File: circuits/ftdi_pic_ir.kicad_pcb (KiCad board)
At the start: 2 copper layers, 33 x 45.7 mm, 20 parts, among them P1 CONN_6, P2 CONN_2, P3 CONN_2, P4 CONN_2, P5 CONN_2, Q1 MOSFET_N, Q2 MOSFET_N, U1 PIC12F683

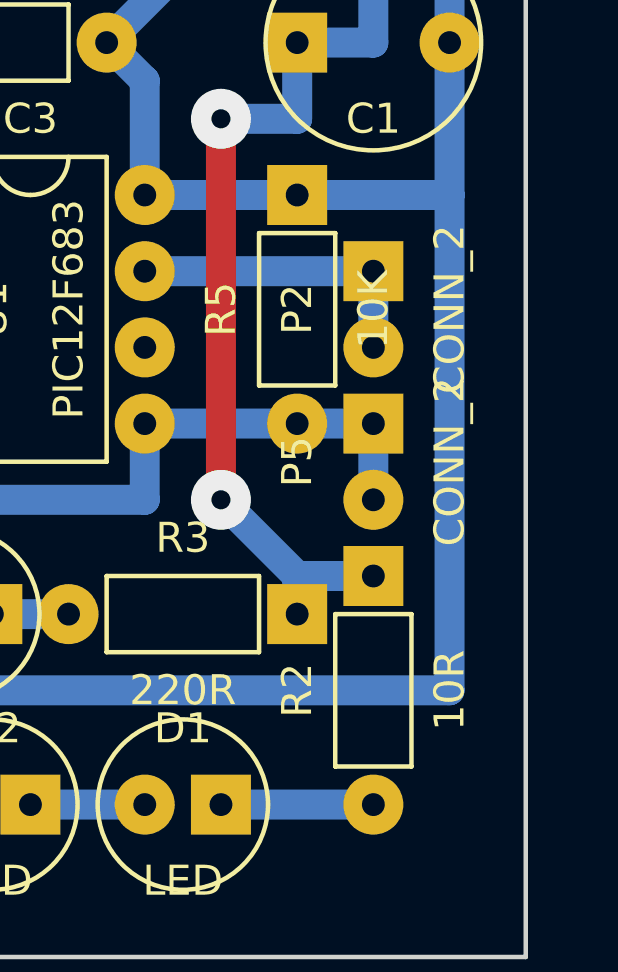
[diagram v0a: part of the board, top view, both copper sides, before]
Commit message: Added ground clip to PIC circuit
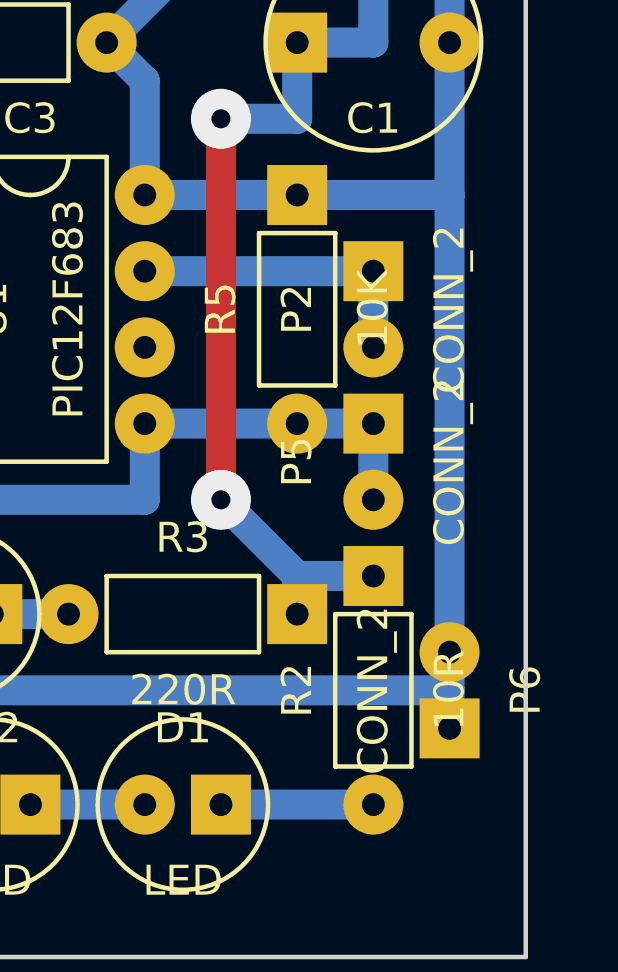
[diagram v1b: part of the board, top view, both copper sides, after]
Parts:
- added P6: CONN_2, CHUNKY_AXIAL-2, F.Cu at (262.9, 111.8)
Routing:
- net GND: track 85.9 -> 87.2 mm

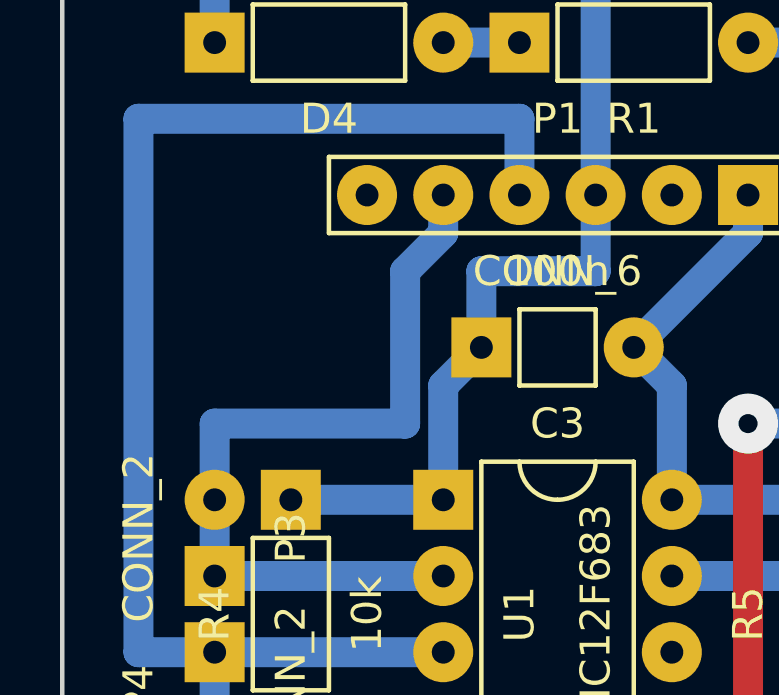
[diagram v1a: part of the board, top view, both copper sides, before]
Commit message: Moved a track on PIC circuit
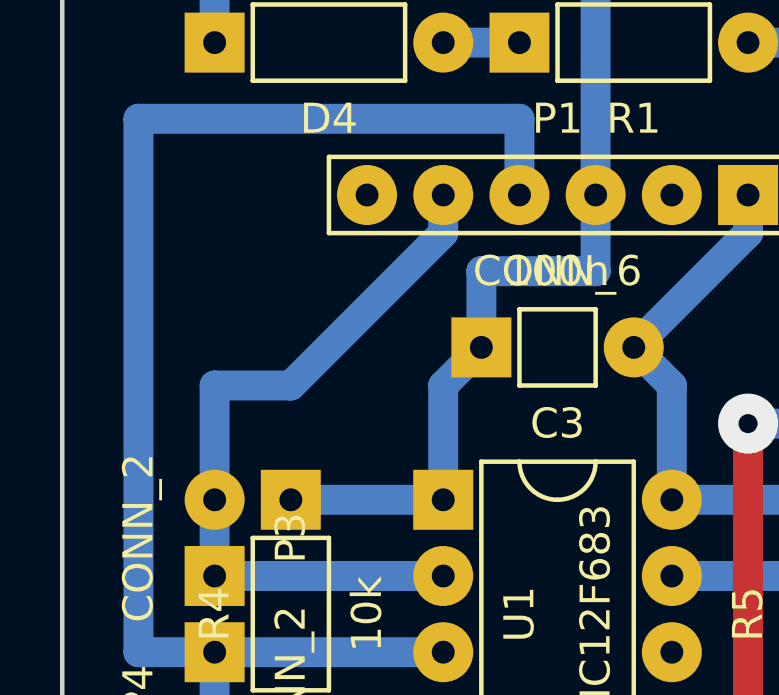
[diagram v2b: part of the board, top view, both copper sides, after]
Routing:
- net FTDI_RX__PIC_TX: track 27.2 -> 25.0 mm
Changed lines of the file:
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@@
     (links 37)
     (no_connects 0)
-    (area 232.334999 74.854999 265.505001 120.725001)
+    (area 232.334999 74.854999 266.205 120.725001)
     (thickness 1.6)
     (drawings 4)
-    (tracks 68)
+    (tracks 67)
     (zones 0)
     (modules 21)
@@
     (visible_elements 7FFFFFFF)
     (pcbplotparams
-      (layerselection 3178497)
-      (usegerberextensions true)
-      (excludeedgelayer true)
+      (layerselection 1)
+      (usegerberextensions false)
+      (excludeedgelayer false)
       (linewidth 0.100000)
       (plotframeref false)
@@
       (padsonsilk false)
       (subtractmaskfromsilk false)
-      (outputformat 1)
+      (outputformat 2)
       (mirror false)
-      (drillshape 1)
+      (drillshape 2)
       (scaleselection 1)
       (outputdirectory ""))
@@
   (segment (start 245.11 91.44) (end 246.38 90.17) (width 1) (layer B.Cu) (net 1))
   (segment (start 245.11 95.25) (end 240.03 95.25) (width 1) (layer B.Cu) (net 1))
-  (segment (start 237.49 95.25) (end 237.49 92.71) (width 1) (layer B.Cu) (net 2))
-  (segment (start 245.11 86.36) (end 245.11 85.09) (width 1) (layer B.Cu) (net 2))
-  (segment (start 243.84 87.63) (end 245.11 86.36) (width 1) (layer B.Cu) (net 2))
-  (segment (start 243.84 92.71) (end 243.84 87.63) (width 1) (layer B.Cu) (net 2))
-  (segment (start 237.49 92.71) (end 243.84 92.71) (width 1) (layer B.Cu) (net 2))
+  (segment (start 245.11 85.09) (end 245.11 86.36) (width 1) (layer B.Cu) (net 2) (status 400000))
+  (segment (start 237.49 91.44) (end 237.49 95.25) (width 1) (layer B.Cu) (net 2) (status 800000))
+  (segment (start 240.03 91.44) (end 237.49 91.44) (width 1) (layer B.Cu) (net 2))
+  (segment (start 245.11 86.36) (end 240.03 91.44) (width 1) (layer B.Cu) (net 2))
   (segment (start 245.11 97.79) (end 237.49 97.79) (width 1) (layer B.Cu) (net 2))
   (segment (start 237.49 97.79) (end 237.49 95.25) (width 1) (layer B.Cu) (net 2))
